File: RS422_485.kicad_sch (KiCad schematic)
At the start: 10 parts, among them U1903 THVD1424

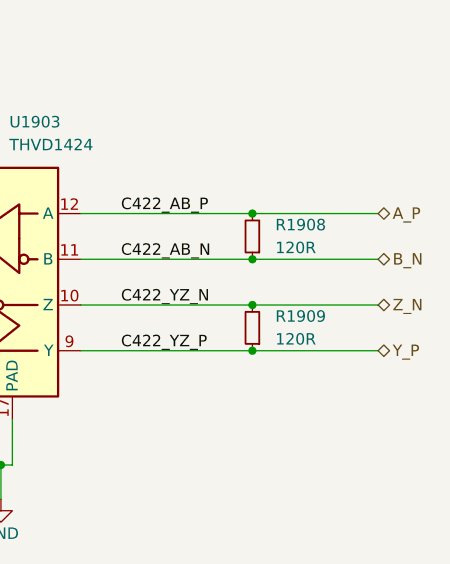
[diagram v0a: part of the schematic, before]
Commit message: added RS422, housekeeping
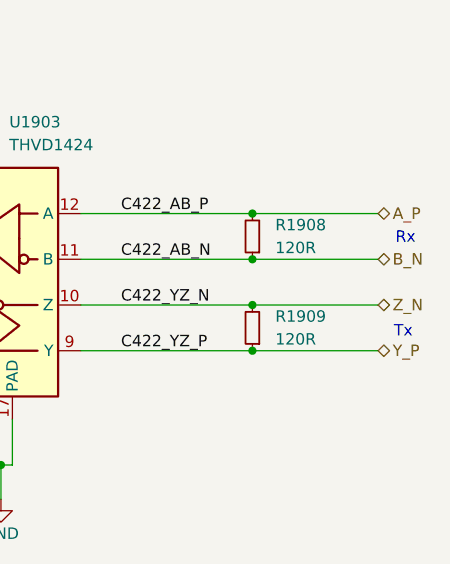
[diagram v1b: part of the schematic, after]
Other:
- note added: "Rx"
- note added: "Tx"
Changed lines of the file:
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@@
 	(generator_version "9.0")
 	(paper "A4")
+	(text "Tx"
+		(exclude_from_sim no)
+		(at 233.934 109.728 0)
+		(effects
+			(font
+				(size 1.27 1.27)
+			)
+		)
+	)
+	(text "Rx"
+		(exclude_from_sim no)
+		(at 234.188 99.314 0)
+		(effects
+			(font
+				(size 1.27 1.27)
+			)
+		)
+	)
 	(text "SLR: log1 = slow\n"
 		(exclude_from_sim no)

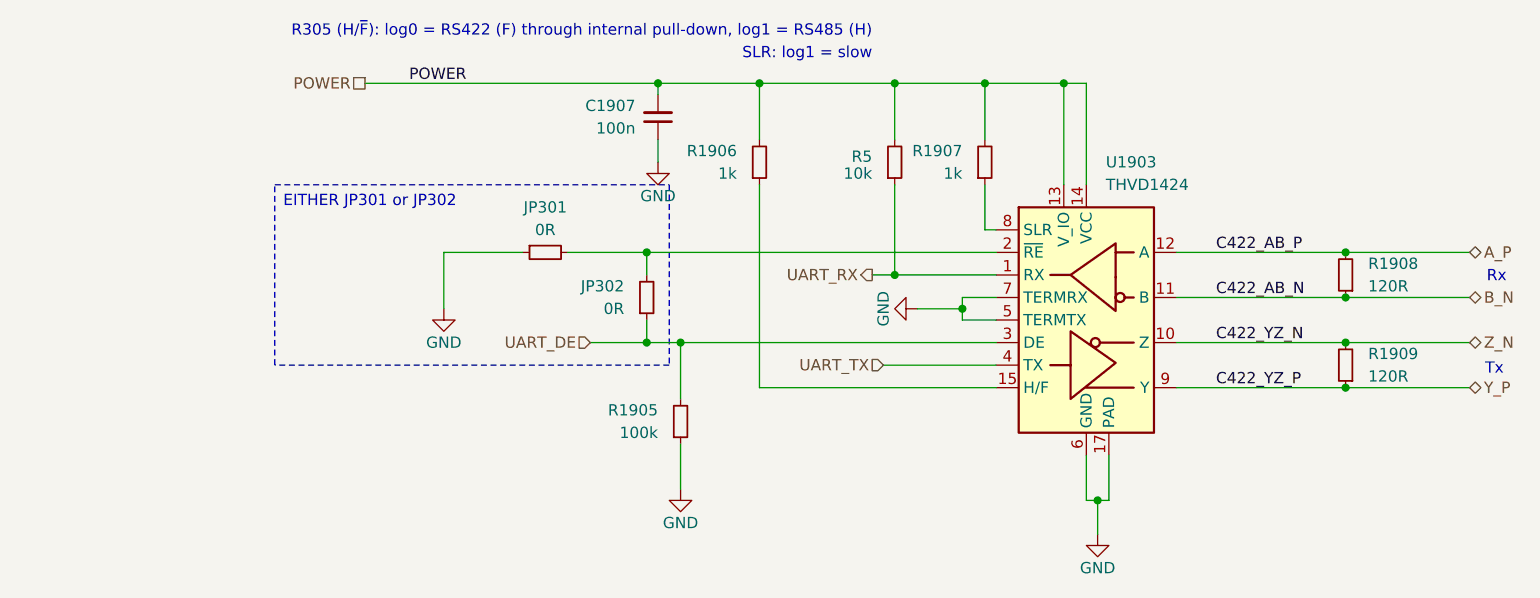
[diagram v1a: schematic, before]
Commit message: updated battery pack module; updated solar inputs module
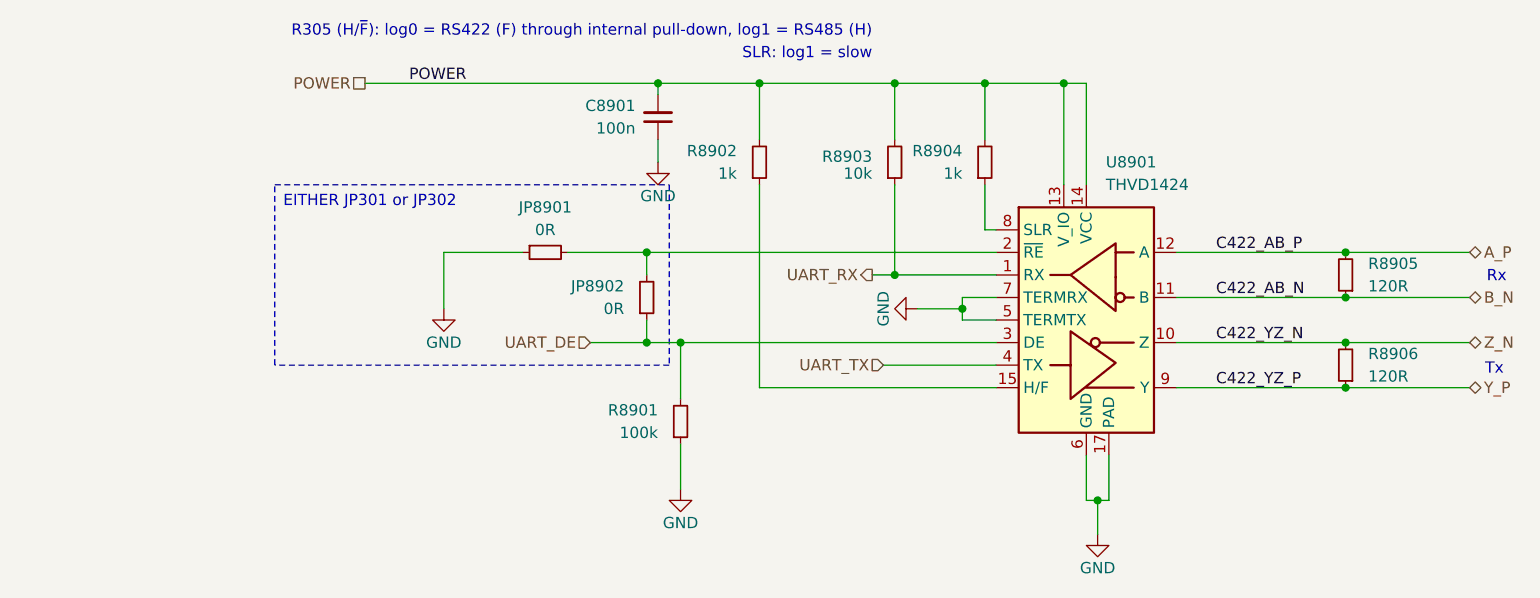
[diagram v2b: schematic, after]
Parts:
- renumbered C1907 to C8901, JP301 to JP8901, JP302 to JP8902, R1905 to R8901, R1906 to R8902, R5 to R8903, R1907 to R8904, R1908 to R8905, R1909 to R8906, U1903 to U8901
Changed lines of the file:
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@@
 		(on_board yes)
 		(dnp no)
-		(property "Reference" "R1908"
+		(property "Reference" "R8905"
 			(at 219.71 97.7899 0)
 			(effects
@@
 			(project "EPS"
 				(path "/94201994-47b8-4213-8d1a-05da12b2a7b0/436fb79f-2d07-4207-b819-4d05a5fd951c/d6499537-8df6-4a5a-92df-5b43e72050a8"
-					(reference "R1908")
+					(reference "R8905")
 					(unit 1)
 				)
@@
 		(on_board yes)
 		(dnp no)
-		(property "Reference" "R5"
+		(property "Reference" "R8903"
 			(at 163.83 85.725 0)
 			(effects
@@
 			(project "EPS"
 				(path "/94201994-47b8-4213-8d1a-05da12b2a7b0/436fb79f-2d07-4207-b819-4d05a5fd951c/d6499537-8df6-4a5a-92df-5b43e72050a8"
-					(reference "R5")
+					(reference "R8903")
 					(unit 1)
 				)
@@
 		(dnp no)
 		(fields_autoplaced yes)
-		(property "Reference" "JP301"
+		(property "Reference" "JP8901"
 			(at 127 91.44 90)
 			(effects
@@
 			(project "EPS"
 				(path "/94201994-47b8-4213-8d1a-05da12b2a7b0/436fb79f-2d07-4207-b819-4d05a5fd951c/d6499537-8df6-4a5a-92df-5b43e72050a8"
-					(reference "JP301")
+					(reference "JP8901")
 					(unit 1)
 				)
@@
 		(on_board yes)
 		(dnp no)
-		(property "Reference" "#PWR01923"
+		(property "Reference" "#PWR08903"
 			(at 142.24 129.54 0)
 			(effects
@@
 			(project "EPS"
 				(path "/94201994-47b8-4213-8d1a-05da12b2a7b0/436fb79f-2d07-4207-b819-4d05a5fd951c/d6499537-8df6-4a5a-92df-5b43e72050a8"
-					(reference "#PWR01923")
+					(reference "#PWR08903")
 					(unit 1)
 				)
@@
 		(dnp no)
 		(fields_autoplaced yes)
-		(property "Reference" "C1907"
+		(property "Reference" "C8901"
 			(at 137.16 80.0035 0)
 			(effects
@@
 			(project "EPS"
 				(path "/94201994-47b8-4213-8d1a-05da12b2a7b0/436fb79f-2d07-4207-b819-4d05a5fd951c/d6499537-8df6-4a5a-92df-5b43e72050a8"
-					(reference "C1907")
+					(reference "C8901")
 					(unit 1)
 				)
@@
 		(dnp no)
 		(fields_autoplaced yes)
-		(property "Reference" "R1906"
+		(property "Reference" "R8902"
 			(at 148.59 85.09 0)
 			(effects
@@
 			(project "EPS"
 				(path "/94201994-47b8-4213-8d1a-05da12b2a7b0/436fb79f-2d07-4207-b819-4d05a5fd951c/d6499537-8df6-4a5a-92df-5b43e72050a8"
-					(reference "R1906")
+					(reference "R8902")
 					(unit 1)
 				)
@@
 		(on_board yes)
 		(dnp no)
-		(property "Reference" "#PWR01925"
+		(property "Reference" "#PWR08905"
 			(at 189.23 134.62 0)
 			(effects
@@
 			(project "EPS"
 				(path "/94201994-47b8-4213-8d1a-05da12b2a7b0/436fb79f-2d07-4207-b819-4d05a5fd951c/d6499537-8df6-4a5a-92df-5b43e72050a8"
-					(reference "#PWR01925")
+					(reference "#PWR08905")
 					(unit 1)
 				)
@@
 		(dnp no)
 		(fields_autoplaced yes)
-		(property "Reference" "R1907"
+		(property "Reference" "R8904"
 			(at 173.99 85.09 0)
 			(effects
@@
 			(project "EPS"
 				(path "/94201994-47b8-4213-8d1a-05da12b2a7b0/436fb79f-2d07-4207-b819-4d05a5fd951c/d6499537-8df6-4a5a-92df-5b43e72050a8"
-					(reference "R1907")
+					(reference "R8904")
 					(unit 1)
 				)
@@
 		(on_board yes)
 		(dnp no)
-		(property "Reference" "#PWR01921"
+		(property "Reference" "#PWR08901"
 			(at 115.57 109.22 0)
 			(effects
@@
 			(project "EPS"
 				(path "/94201994-47b8-4213-8d1a-05da12b2a7b0/436fb79f-2d07-4207-b819-4d05a5fd951c/d6499537-8df6-4a5a-92df-5b43e72050a8"
-					(reference "#PWR01921")
+					(reference "#PWR08901")
 					(unit 1)
 				)
@@
 		(dnp no)
 		(fields_autoplaced yes)
-		(property "Reference" "R1905"
+		(property "Reference" "R8901"
 			(at 139.7 114.2999 0)
 			(effects
@@
 			(project "EPS"
 				(path "/94201994-47b8-4213-8d1a-05da12b2a7b0/436fb79f-2d07-4207-b819-4d05a5fd951c/d6499537-8df6-4a5a-92df-5b43e72050a8"
-					(reference "R1905")
+					(reference "R8901")
 					(unit 1)
 				)
@@
 		(dnp no)
 		(fields_autoplaced yes)
-		(property "Reference" "U1903"
+		(property "Reference" "U8901"
 			(at 190.1541 86.36 0)
 			(effects
@@
 			(project "EPS"
 				(path "/94201994-47b8-4213-8d1a-05da12b2a7b0/436fb79f-2d07-4207-b819-4d05a5fd951c/d6499537-8df6-4a5a-92df-5b43e72050a8"
-					(reference "U1903")
+					(reference "U8901")
 					(unit 1)
 				)
@@
 		(on_board yes)
 		(dnp no)
-		(property "Reference" "#PWR01924"
+		(property "Reference" "#PWR08904"
 			(at 162.56 102.87 0)
 			(effects
@@
 			(project "EPS"
 				(path "/94201994-47b8-4213-8d1a-05da12b2a7b0/436fb79f-2d07-4207-b819-4d05a5fd951c/d6499537-8df6-4a5a-92df-5b43e72050a8"
-					(reference "#PWR01924")
+					(reference "#PWR08904")
 					(unit 1)
 				)
@@
 		(on_board yes)
 		(dnp no)
-		(property "Reference" "R1909"
+		(property "Reference" "R8906"
 			(at 219.71 107.9499 0)
 			(effects
@@
 			(project "EPS"
 				(path "/94201994-47b8-4213-8d1a-05da12b2a7b0/436fb79f-2d07-4207-b819-4d05a5fd951c/d6499537-8df6-4a5a-92df-5b43e72050a8"
-					(reference "R1909")
+					(reference "R8906")
 					(unit 1)
 				)
@@
 		(on_board yes)
 		(dnp no)
-		(property "Reference" "#PWR01922"
+		(property "Reference" "#PWR08902"
 			(at 139.7 92.71 0)
 			(effects
@@
 			(project "EPS"
 				(path "/94201994-47b8-4213-8d1a-05da12b2a7b0/436fb79f-2d07-4207-b819-4d05a5fd951c/d6499537-8df6-4a5a-92df-5b43e72050a8"
-					(reference "#PWR01922")
+					(reference "#PWR08902")
 					(unit 1)
 				)
@@
 		(dnp no)
 		(fields_autoplaced yes)
-		(property "Reference" "JP302"
+		(property "Reference" "JP8902"
 			(at 135.89 100.33 0)
 			(effects
@@
 			(project "EPS"
 				(path "/94201994-47b8-4213-8d1a-05da12b2a7b0/436fb79f-2d07-4207-b819-4d05a5fd951c/d6499537-8df6-4a5a-92df-5b43e72050a8"
-					(reference "JP302")
-					(unit 1)
-				)
+					(reference "JP8902")
+					(unit 1)
+				)

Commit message: wired channel alerts; added schematic for test pbc
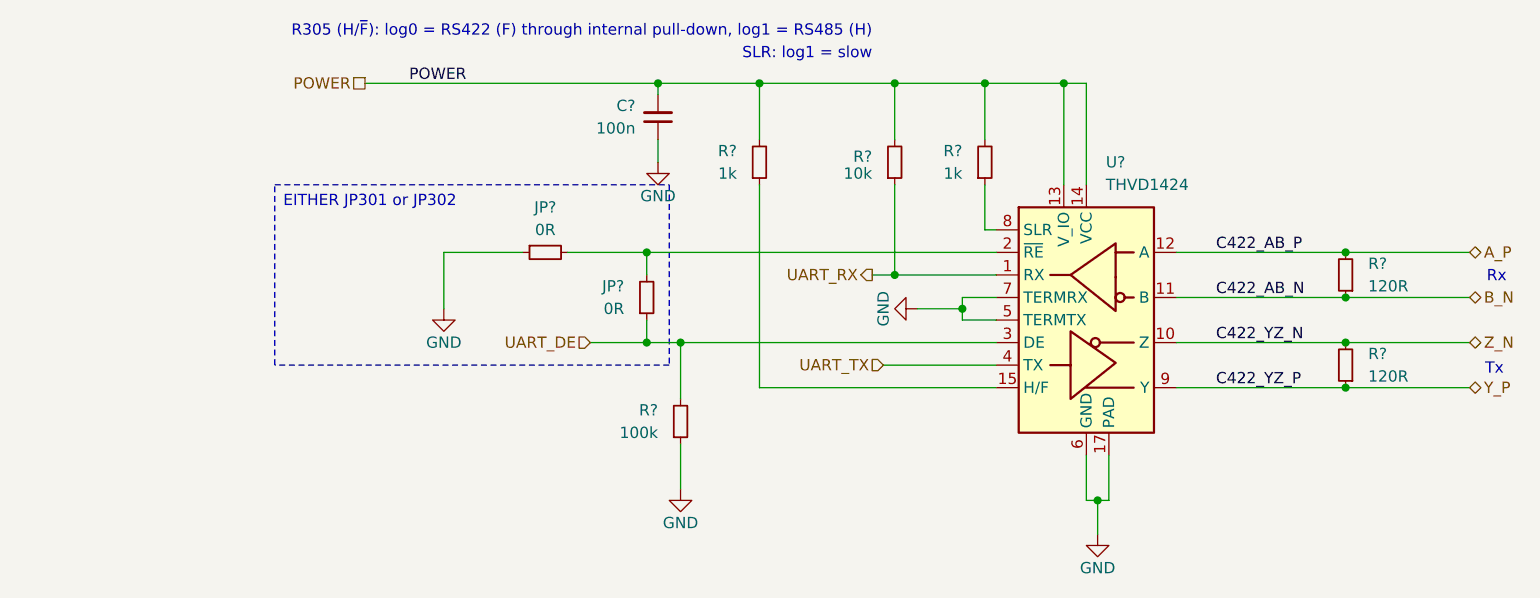
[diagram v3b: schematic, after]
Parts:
- renumbered C8901 to C?, JP8901 to JP?, JP8902 to JP?, R8905 to R?, R8903 to R?, R8902 to R?, R8904 to R?, R8901 to R?, R8906 to R?, U8901 to U?
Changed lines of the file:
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@@
 		(on_board yes)
 		(dnp no)
-		(property "Reference" "R8905"
+		(property "Reference" "R?"
 			(at 219.71 97.7899 0)
 			(effects
@@
 		)
 		(instances
+			(project "TEST_PCB"
+				(path "/29496ace-b476-4f24-a65f-9da1dd70122c/3917d7ef-211e-46e0-b3be-0af8f01be35a/d6499537-8df6-4a5a-92df-5b43e72050a8"
+					(reference "R?")
+					(unit 1)
+				)
+			)
 			(project "EPS"
 				(path "/94201994-47b8-4213-8d1a-05da12b2a7b0/436fb79f-2d07-4207-b819-4d05a5fd951c/d6499537-8df6-4a5a-92df-5b43e72050a8"
@@
 		(on_board yes)
 		(dnp no)
-		(property "Reference" "R8903"
+		(property "Reference" "R?"
 			(at 163.83 85.725 0)
 			(effects
@@
 		)
 		(instances
+			(project "TEST_PCB"
+				(path "/29496ace-b476-4f24-a65f-9da1dd70122c/3917d7ef-211e-46e0-b3be-0af8f01be35a/d6499537-8df6-4a5a-92df-5b43e72050a8"
+					(reference "R?")
+					(unit 1)
+				)
+			)
 			(project "EPS"
 				(path "/94201994-47b8-4213-8d1a-05da12b2a7b0/436fb79f-2d07-4207-b819-4d05a5fd951c/d6499537-8df6-4a5a-92df-5b43e72050a8"
@@
 		(dnp no)
 		(fields_autoplaced yes)
-		(property "Reference" "JP8901"
+		(property "Reference" "JP?"
 			(at 127 91.44 90)
 			(effects
@@
 		)
 		(instances
+			(project "TEST_PCB"
+				(path "/29496ace-b476-4f24-a65f-9da1dd70122c/3917d7ef-211e-46e0-b3be-0af8f01be35a/d6499537-8df6-4a5a-92df-5b43e72050a8"
+					(reference "JP?")
+					(unit 1)
+				)
+			)
 			(project "EPS"
 				(path "/94201994-47b8-4213-8d1a-05da12b2a7b0/436fb79f-2d07-4207-b819-4d05a5fd951c/d6499537-8df6-4a5a-92df-5b43e72050a8"
@@
 		(on_board yes)
 		(dnp no)
-		(property "Reference" "#PWR08903"
+		(property "Reference" "#PWR?"
 			(at 142.24 129.54 0)
 			(effects
@@
 		)
 		(instances
+			(project "TEST_PCB"
+				(path "/29496ace-b476-4f24-a65f-9da1dd70122c/3917d7ef-211e-46e0-b3be-0af8f01be35a/d6499537-8df6-4a5a-92df-5b43e72050a8"
+					(reference "#PWR?")
+					(unit 1)
+				)
+			)
 			(project "EPS"
 				(path "/94201994-47b8-4213-8d1a-05da12b2a7b0/436fb79f-2d07-4207-b819-4d05a5fd951c/d6499537-8df6-4a5a-92df-5b43e72050a8"
@@
 		(dnp no)
 		(fields_autoplaced yes)
-		(property "Reference" "C8901"
+		(property "Reference" "C?"
 			(at 137.16 80.0035 0)
 			(effects
@@
 		)
 		(instances
+			(project "TEST_PCB"
+				(path "/29496ace-b476-4f24-a65f-9da1dd70122c/3917d7ef-211e-46e0-b3be-0af8f01be35a/d6499537-8df6-4a5a-92df-5b43e72050a8"
+					(reference "C?")
+					(unit 1)
+				)
+			)
 			(project "EPS"
 				(path "/94201994-47b8-4213-8d1a-05da12b2a7b0/436fb79f-2d07-4207-b819-4d05a5fd951c/d6499537-8df6-4a5a-92df-5b43e72050a8"
@@
 		(dnp no)
 		(fields_autoplaced yes)
-		(property "Reference" "R8902"
+		(property "Reference" "R?"
 			(at 148.59 85.09 0)
 			(effects
@@
 		)
 		(instances
+			(project "TEST_PCB"
+				(path "/29496ace-b476-4f24-a65f-9da1dd70122c/3917d7ef-211e-46e0-b3be-0af8f01be35a/d6499537-8df6-4a5a-92df-5b43e72050a8"
+					(reference "R?")
+					(unit 1)
+				)
+			)
 			(project "EPS"
 				(path "/94201994-47b8-4213-8d1a-05da12b2a7b0/436fb79f-2d07-4207-b819-4d05a5fd951c/d6499537-8df6-4a5a-92df-5b43e72050a8"
@@
 		(on_board yes)
 		(dnp no)
-		(property "Reference" "#PWR08905"
+		(property "Reference" "#PWR?"
 			(at 189.23 134.62 0)
 			(effects
@@
 		)
 		(instances
+			(project "TEST_PCB"
+				(path "/29496ace-b476-4f24-a65f-9da1dd70122c/3917d7ef-211e-46e0-b3be-0af8f01be35a/d6499537-8df6-4a5a-92df-5b43e72050a8"
+					(reference "#PWR?")
+					(unit 1)
+				)
+			)
 			(project "EPS"
 				(path "/94201994-47b8-4213-8d1a-05da12b2a7b0/436fb79f-2d07-4207-b819-4d05a5fd951c/d6499537-8df6-4a5a-92df-5b43e72050a8"
@@
 		(dnp no)
 		(fields_autoplaced yes)
-		(property "Reference" "R8904"
+		(property "Reference" "R?"
 			(at 173.99 85.09 0)
 			(effects
@@
 		)
 		(instances
+			(project "TEST_PCB"
+				(path "/29496ace-b476-4f24-a65f-9da1dd70122c/3917d7ef-211e-46e0-b3be-0af8f01be35a/d6499537-8df6-4a5a-92df-5b43e72050a8"
+					(reference "R?")
+					(unit 1)
+				)
+			)
 			(project "EPS"
 				(path "/94201994-47b8-4213-8d1a-05da12b2a7b0/436fb79f-2d07-4207-b819-4d05a5fd951c/d6499537-8df6-4a5a-92df-5b43e72050a8"
@@
 		(on_board yes)
 		(dnp no)
-		(property "Reference" "#PWR08901"
+		(property "Reference" "#PWR?"
 			(at 115.57 109.22 0)
 			(effects
@@
 		)
 		(instances
+			(project "TEST_PCB"
+				(path "/29496ace-b476-4f24-a65f-9da1dd70122c/3917d7ef-211e-46e0-b3be-0af8f01be35a/d6499537-8df6-4a5a-92df-5b43e72050a8"
+					(reference "#PWR?")
+					(unit 1)
+				)
+			)
 			(project "EPS"
 				(path "/94201994-47b8-4213-8d1a-05da12b2a7b0/436fb79f-2d07-4207-b819-4d05a5fd951c/d6499537-8df6-4a5a-92df-5b43e72050a8"
@@
 		(dnp no)
 		(fields_autoplaced yes)
-		(property "Reference" "R8901"
+		(property "Reference" "R?"
 			(at 139.7 114.2999 0)
 			(effects
@@
 		)
 		(instances
+			(project "TEST_PCB"
+				(path "/29496ace-b476-4f24-a65f-9da1dd70122c/3917d7ef-211e-46e0-b3be-0af8f01be35a/d6499537-8df6-4a5a-92df-5b43e72050a8"
+					(reference "R?")
+					(unit 1)
+				)
+			)
 			(project "EPS"
 				(path "/94201994-47b8-4213-8d1a-05da12b2a7b0/436fb79f-2d07-4207-b819-4d05a5fd951c/d6499537-8df6-4a5a-92df-5b43e72050a8"
@@
 		(dnp no)
 		(fields_autoplaced yes)
-		(property "Reference" "U8901"
+		(property "Reference" "U?"
 			(at 190.1541 86.36 0)
 			(effects
@@
 		)
 		(instances
+			(project "TEST_PCB"
+				(path "/29496ace-b476-4f24-a65f-9da1dd70122c/3917d7ef-211e-46e0-b3be-0af8f01be35a/d6499537-8df6-4a5a-92df-5b43e72050a8"
+					(reference "U?")
+					(unit 1)
+				)
+			)
 			(project "EPS"
 				(path "/94201994-47b8-4213-8d1a-05da12b2a7b0/436fb79f-2d07-4207-b819-4d05a5fd951c/d6499537-8df6-4a5a-92df-5b43e72050a8"
@@
 		(on_board yes)
 		(dnp no)
-		(property "Reference" "#PWR08904"
+		(property "Reference" "#PWR?"
 			(at 162.56 102.87 0)
 			(effects
@@
 		)
 		(instances
+			(project "TEST_PCB"
+				(path "/29496ace-b476-4f24-a65f-9da1dd70122c/3917d7ef-211e-46e0-b3be-0af8f01be35a/d6499537-8df6-4a5a-92df-5b43e72050a8"
+					(reference "#PWR?")
+					(unit 1)
+				)
+			)
 			(project "EPS"
 				(path "/94201994-47b8-4213-8d1a-05da12b2a7b0/436fb79f-2d07-4207-b819-4d05a5fd951c/d6499537-8df6-4a5a-92df-5b43e72050a8"
@@
 		(on_board yes)
 		(dnp no)
-		(property "Reference" "R8906"
+		(property "Reference" "R?"
 			(at 219.71 107.9499 0)
 			(effects
@@
 		)
 		(instances
+			(project "TEST_PCB"
+				(path "/29496ace-b476-4f24-a65f-9da1dd70122c/3917d7ef-211e-46e0-b3be-0af8f01be35a/d6499537-8df6-4a5a-92df-5b43e72050a8"
+					(reference "R?")
+					(unit 1)
+				)
+			)
 			(project "EPS"
 				(path "/94201994-47b8-4213-8d1a-05da12b2a7b0/436fb79f-2d07-4207-b819-4d05a5fd951c/d6499537-8df6-4a5a-92df-5b43e72050a8"
@@
 		(on_board yes)
 		(dnp no)
-		(property "Reference" "#PWR08902"
+		(property "Reference" "#PWR?"
 			(at 139.7 92.71 0)
 			(effects
@@
 		)
 		(instances
+			(project "TEST_PCB"
+				(path "/29496ace-b476-4f24-a65f-9da1dd70122c/3917d7ef-211e-46e0-b3be-0af8f01be35a/d6499537-8df6-4a5a-92df-5b43e72050a8"
+					(reference "#PWR?")
+					(unit 1)
+				)
+			)
 			(project "EPS"
 				(path "/94201994-47b8-4213-8d1a-05da12b2a7b0/436fb79f-2d07-4207-b819-4d05a5fd951c/d6499537-8df6-4a5a-92df-5b43e72050a8"
@@
 		(dnp no)
 		(fields_autoplaced yes)
-		(property "Reference" "JP8902"
+		(property "Reference" "JP?"
 			(at 135.89 100.33 0)
 			(effects
@@
 		)
 		(instances
-			(project "EPS"
-				(path "/94201994-47b8-4213-8d1a-05da12b2a7b0/436fb79f-2d07-4207-b819-4d05a5fd951c/d6499537-8df6-4a5a-92df-5b43e72050a8"
+			(project "TEST_PCB"
+				(path "/29496ace-b476-4f24-a65f-9da1dd70122c/3917d7ef-211e-46e0-b3be-0af8f01be35a/d6499537-8df6-4a5a-92df-5b43e72050a8"
+					(reference "JP?")
+					(unit 1)
+				)
+			)
+			(project "EPS"
+				(path "/94201994-47b8-4213-8d1a-05da12b2a7b0/436fb79f-2d07-4207-b819-4d05a5fd951c/d6499537-8df6-4a5a-92df-5b43e72050a8"

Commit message: reduced number of DCDC converter for PV panels; updated test pcb
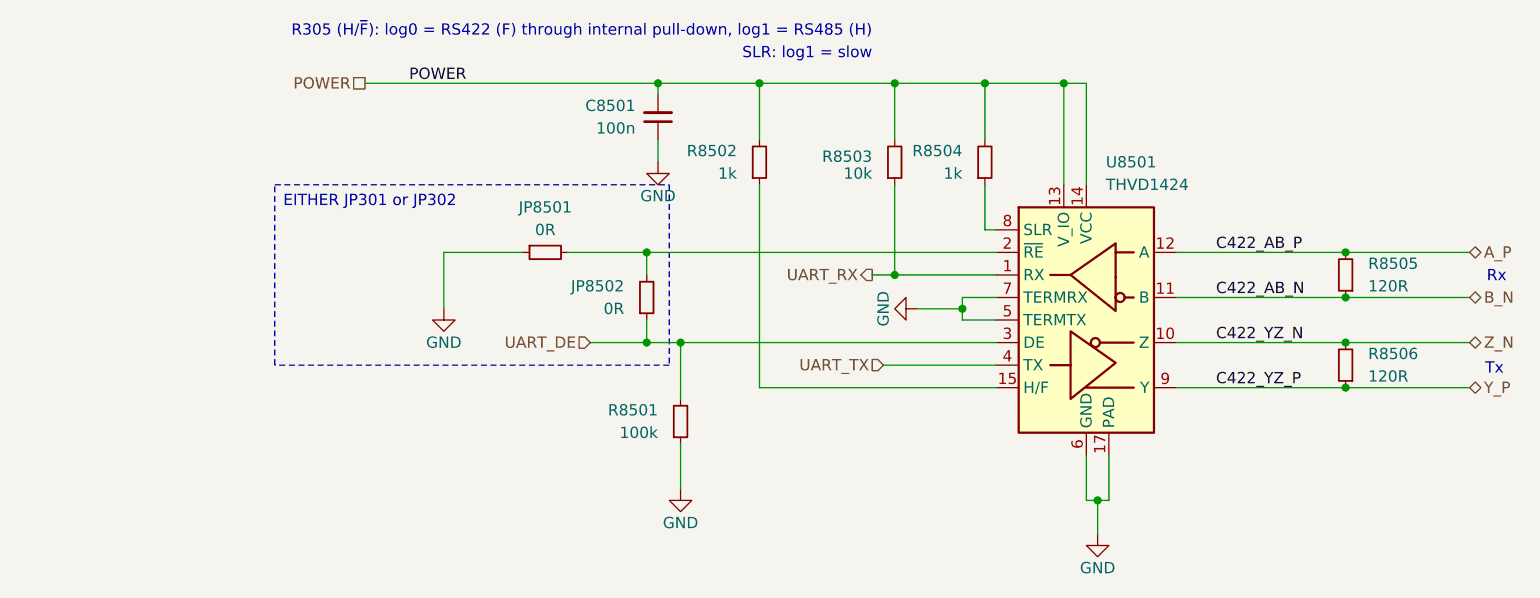
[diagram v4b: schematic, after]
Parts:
- gave numbers to parts that had none: 10
